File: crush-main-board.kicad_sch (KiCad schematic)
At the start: 25 parts, among them J1 4x4_Header, J10 3x3 Header, J11 3x3 Header, J12 3x2 Header, J13 3x4_Header, J14 3x4_Header, J15 2157601008, J16 Conn_01x02, J17 Conn_01x02, J2 4x4_Header, J3 6x2_Header, J4 3x1_Header, J5 3x2 Header, J6 3x2 Header, J7 3x4 Header, J8 3x4 Header, J9 3x3 Header, U1 Teensy4.1, U2 ISO7740DW, U3 ISO7740DW

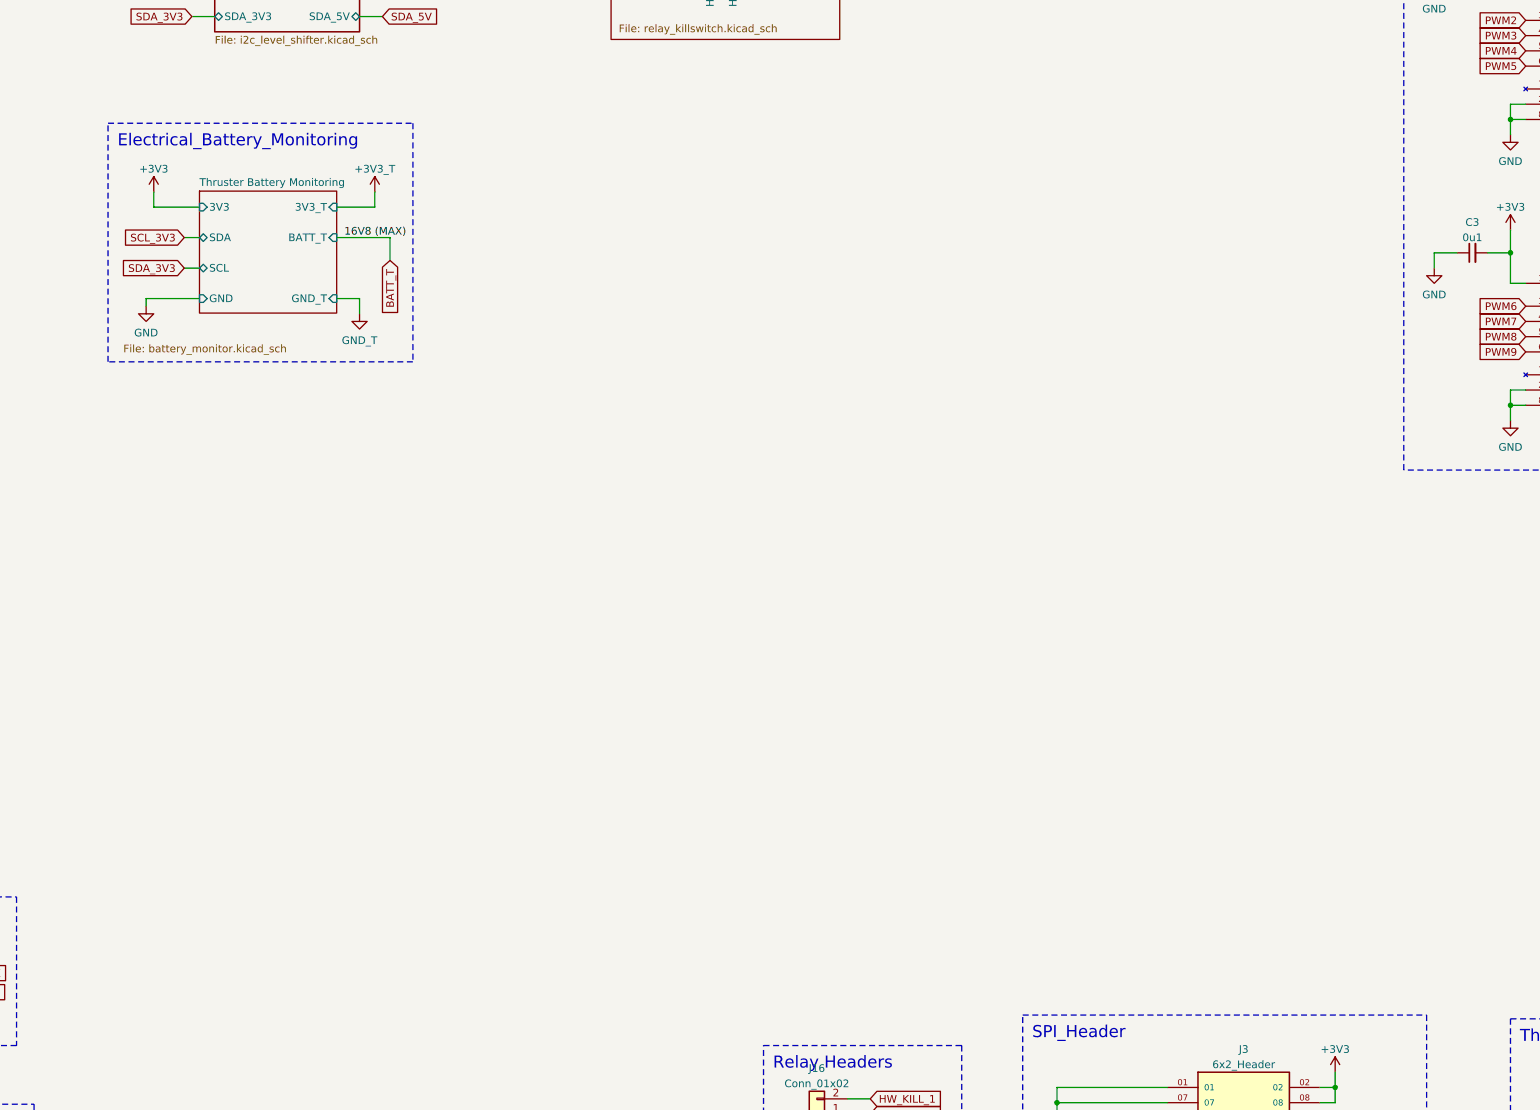
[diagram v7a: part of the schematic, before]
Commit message: Add monitor for signal battery
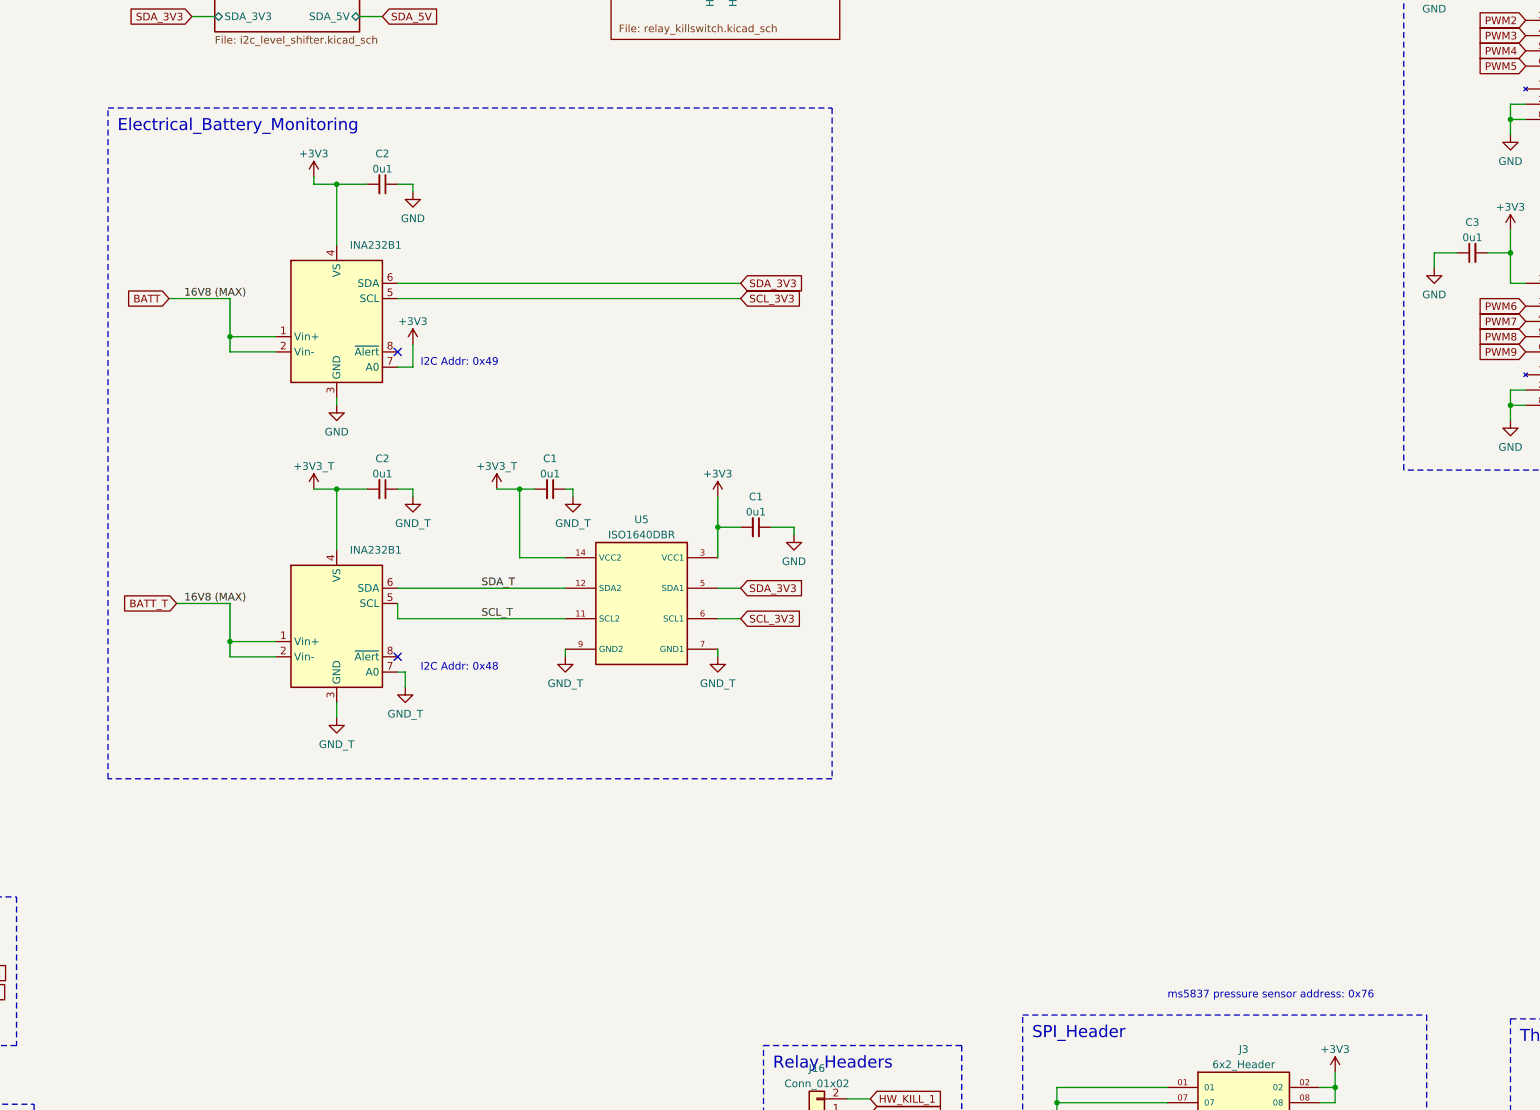
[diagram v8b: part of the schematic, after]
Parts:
- added C1 (x2), C2 (x2): 0u1, Capacitor_SMD:C_0603_1608Metric_Pad1.08x0.95mm_HandSolder, symbol Device:C_Small
- added INA232B1 (x2): ~, Package_TO_SOT_SMD:SOT-23-8_Handsoldering, symbol Crush_MainBoard_Symbols:INA232
- added U5: ISO1640DBR, Crush_Mainboard_Footprints:SOIC127P1030X265-16N, symbol Crush_MainBoard_Symbols:ISO1640DBR
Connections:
- net BATT_T is gone; now on net BATT: J15.6
- net +3V3: now also C1.2, C2.2, INA232B1.4 (VS), INA232B1.7 (A0), U5.3 (VCC1)
- net +3V3_T: now also C1.2, C2.2, INA232B1.4 (VS), U5.14 (VCC2)
- net BATT: now also INA232B1.1 (Vin+), INA232B1.1 (Vin+), INA232B1.2 (Vin-), INA232B1.2 (Vin-)
- net GND: now also C1.1, C2.1, INA232B1.3 (GND)
- net GND_T: now also C1.1, C2.1, INA232B1.3 (GND), INA232B1.7 (A0), U5.7 (GND1), U5.9 (GND2)
- net SCL_3V3: now also INA232B1.5 (SCL), U5.6 (SCL1)
- net SDA_3V3: now also INA232B1.6 (SDA), U5.5 (SDA1)
- new net SCL_T: INA232B1.5 (SCL), U5.11 (SCL2)
- new net SDA_T: INA232B1.6 (SDA), U5.12 (SDA2)
- no-connect marks 19 -> 21
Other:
- removed sheet Thruster Battery Monitoring
- note added: "I2C Addr: 0x48"
- note added: "I2C Addr: 0x49"
- note added: "ms5837 pressure sensor address: 0x76"
